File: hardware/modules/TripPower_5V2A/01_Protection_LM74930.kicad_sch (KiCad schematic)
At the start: 41 parts, among them J301 INPUT: VIN/RUN/GND, J302 OUT: PROT_UNFUSED/5V/GND, Q301 SQM10250E_GE3 250V CANDIDATE, Q302 BUK7Y4R8-60EX 60V CANDIDATE, U301 LM74930QRGERQ1

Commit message: feat(TripPower REV5): repurpose R317/R319 for RUN/AUTO sense; DNP legacy PNP EN path and BAS116
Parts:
- D305: value BAS116Q-7-F SERIES RUN SINK NO USB BACKFEED -> REV5 DNP LEGACY D305; now not fitted
- R316: value 22k EN PULLDOWN - VS ONLY PNP -> REV5 DNP LEGACY R316; now not fitted
- R317: value 4.7k RUN SERIES -> 1M 1% RUN_CMD TO SENSE2 - RUN ONLY; MPN (none) -> RC1206FR-071ML
- R318: value 68k PNP OUTPUT CURRENT LIMIT 202V -> REV5 DNP LEGACY R318; now not fitted
- R319: value 0R POPULATE FOR ALWAYS_ON -> 0R AUTO VS TO RUN_SENSE; DNP IN RUN; MPN (none) -> RC1206JR-070RL
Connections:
- net GND: no longer R319.2
- net RUN_BYPASS_NODE: no longer R319.1
- net VS_CLAMP: now also R319.1
- net RUN_BASE renamed RUN_SENSE
- net RUN_SENSE: now also R319.2
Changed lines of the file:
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@@
 (symbol (lib_id "Tripmaster_Sym:R") (at 149.86 275.59 0) (unit 1) (in_bom yes) (on_board yes) (dnp no) (property "Reference" "R314" (at 149.86 261.62 0) (effects (font (size 1 1)))) (property "Value" "3.3k 2512 PULSE CANDIDATE" (at 149.86 264.16 0) (effects (font (size 1 1)))) (property "Footprint" "Resistor_SMD:R_2512_6332Metric" (at 149.86 275.59 0) (effects (font (size 1.0 1.0)) (hide yes))) (property "MPN" "CRCW25123K30FKEGHP" (at 0 0 0) (effects (font (size 1 1)) (hide yes))) (pin "1") (pin "2") (instances (project "TripPower_5V2A" (path "/f1512578-cc72-4c26-bf70-dbbd00000001/f1512578-cc72-4c26-bf70-dbbd00000002" (reference "R314") (unit 1)))))
 (symbol (lib_id "Tripmaster_Sym:R") (at 234.95 275.59 0) (unit 1) (in_bom yes) (on_board yes) (dnp no) (property "Reference" "R315" (at 234.95 261.62 0) (effects (font (size 1 1)))) (property "Value" "3.3k 2512 PULSE CANDIDATE" (at 234.95 264.16 0) (effects (font (size 1 1)))) (property "Footprint" "Resistor_SMD:R_2512_6332Metric" (at 234.95 275.59 0) (effects (font (size 1.0 1.0)) (hide yes))) (property "MPN" "CRCW25123K30FKEGHP" (at 0 0 0) (effects (font (size 1 1)) (hide yes))) (pin "1") (pin "2") (instances (project "TripPower_5V2A" (path "/f1512578-cc72-4c26-bf70-dbbd00000001/f1512578-cc72-4c26-bf70-dbbd00000002" (reference "R315") (unit 1)))))
-(symbol (lib_id "Tripmaster_Sym:R") (at 320.04 275.59 0) (unit 1) (in_bom yes) (on_board yes) (dnp no) (property "Reference" "R316" (at 320.04 261.62 0) (effects (font (size 1 1)))) (property "Value" "22k EN PULLDOWN - VS ONLY PNP" (at 320.04 264.16 0) (effects (font (size 1 1)))) (property "Footprint" "Tripmaster:R_1206_3216" (at 320.04 275.59 0) (effects (font (size 1.0 1.0)) (hide yes))) (pin "1") (pin "2") (instances (project "TripPower_5V2A" (path "/f1512578-cc72-4c26-bf70-dbbd00000001/f1512578-cc72-4c26-bf70-dbbd00000002" (reference "R316") (unit 1)))))
-(symbol (lib_id "Tripmaster_Sym:R") (at 405.13 275.59 0) (unit 1) (in_bom yes) (on_board yes) (dnp no) (property "Reference" "R317" (at 405.13 261.62 0) (effects (font (size 1 1)))) (property "Value" "4.7k RUN SERIES" (at 405.13 264.16 0) (effects (font (size 1 1)))) (property "Footprint" "Tripmaster:R_1206_3216" (at 405.13 275.59 0) (effects (font (size 1.0 1.0)) (hide yes))) (pin "1") (pin "2") (instances (project "TripPower_5V2A" (path "/f1512578-cc72-4c26-bf70-dbbd00000001/f1512578-cc72-4c26-bf70-dbbd00000002" (reference "R317") (unit 1)))))
-(symbol (lib_id "Tripmaster_Sym:R") (at 490.22 275.59 0) (unit 1) (in_bom yes) (on_board yes) (dnp no) (property "Reference" "R318" (at 490.22 261.62 0) (effects (font (size 1 1)))) (property "Value" "68k PNP OUTPUT CURRENT LIMIT 202V" (at 490.22 264.16 0) (effects (font (size 1 1)))) (property "Footprint" "Tripmaster:R_1206_3216" (at 490.22 275.59 0) (effects (font (size 1.0 1.0)) (hide yes))) (pin "1") (pin "2") (instances (project "TripPower_5V2A" (path "/f1512578-cc72-4c26-bf70-dbbd00000001/f1512578-cc72-4c26-bf70-dbbd00000002" (reference "R318") (unit 1)))))
-(symbol (lib_id "Tripmaster_Sym:R") (at 64.77 299.72 0) (unit 1) (in_bom yes) (on_board yes) (dnp no) (property "Reference" "R319" (at 64.77 285.75 0) (effects (font (size 1 1)))) (property "Value" "0R POPULATE FOR ALWAYS_ON" (at 64.77 288.29 0) (effects (font (size 1 1)))) (property "Footprint" "Tripmaster:R_1206_3216" (at 64.77 299.72 0) (effects (font (size 1.0 1.0)) (hide yes))) (pin "1") (pin "2") (instances (project "TripPower_5V2A" (path "/f1512578-cc72-4c26-bf70-dbbd00000001/f1512578-cc72-4c26-bf70-dbbd00000002" (reference "R319") (unit 1)))))
+(symbol (lib_id "Tripmaster_Sym:R") (at 320.04 275.59 0) (unit 1) (in_bom yes) (on_board yes) (dnp yes) (property "Reference" "R316" (at 320.04 261.62 0) (effects (font (size 1 1)))) (property "Value" "REV5 DNP LEGACY R316" (at 320.04 264.16 0) (effects (font (size 1 1)))) (property "Footprint" "Tripmaster:R_1206_3216" (at 320.04 275.59 0) (effects (font (size 1.0 1.0)) (hide yes))) (pin "1") (pin "2") (instances (project "TripPower_5V2A" (path "/f1512578-cc72-4c26-bf70-dbbd00000001/f1512578-cc72-4c26-bf70-dbbd00000002" (reference "R316") (unit 1)))))
+(symbol (lib_id "Tripmaster_Sym:R") (at 405.13 275.59 0) (unit 1) (in_bom yes) (on_board yes) (dnp no) (property "Reference" "R317" (at 405.13 261.62 0) (effects (font (size 1 1)))) (property "Value" "1M 1% RUN_CMD TO SENSE2 - RUN ONLY" (at 405.13 264.16 0) (effects (font (size 1 1)))) (property "Footprint" "Tripmaster:R_1206_3216" (at 405.13 275.59 0) (effects (font (size 1.0 1.0)) (hide yes))) (property "MPN" "RC1206FR-071ML" (at 0 0 0) (effects (font (size 1 1)) (hide yes))) (pin "1") (pin "2") (instances (project "TripPower_5V2A" (path "/f1512578-cc72-4c26-bf70-dbbd00000001/f1512578-cc72-4c26-bf70-dbbd00000002" (reference "R317") (unit 1)))))
+(symbol (lib_id "Tripmaster_Sym:R") (at 490.22 275.59 0) (unit 1) (in_bom yes) (on_board yes) (dnp yes) (property "Reference" "R318" (at 490.22 261.62 0) (effects (font (size 1 1)))) (property "Value" "REV5 DNP LEGACY R318" (at 490.22 264.16 0) (effects (font (size 1 1)))) (property "Footprint" "Tripmaster:R_1206_3216" (at 490.22 275.59 0) (effects (font (size 1.0 1.0)) (hide yes))) (pin "1") (pin "2") (instances (project "TripPower_5V2A" (path "/f1512578-cc72-4c26-bf70-dbbd00000001/f1512578-cc72-4c26-bf70-dbbd00000002" (reference "R318") (unit 1)))))
+(symbol (lib_id "Tripmaster_Sym:R") (at 64.77 299.72 0) (unit 1) (in_bom yes) (on_board yes) (dnp no) (property "Reference" "R319" (at 64.77 285.75 0) (effects (font (size 1 1)))) (property "Value" "0R AUTO VS TO RUN_SENSE; DNP IN RUN" (at 64.77 288.29 0) (effects (font (size 1 1)))) (property "Footprint" "Tripmaster:R_1206_3216" (at 64.77 299.72 0) (effects (font (size 1.0 1.0)) (hide yes))) (property "MPN" "RC1206JR-070RL" (at 0 0 0) (effects (font (size 1 1)) (hide yes))) (pin "1") (pin "2") (instances (project "TripPower_5V2A" (path "/f1512578-cc72-4c26-bf70-dbbd00000001/f1512578-cc72-4c26-bf70-dbbd00000002" (reference "R319") (unit 1)))))
 (symbol (lib_id "Tripmaster_Sym:R") (at 149.86 299.72 0) (unit 1) (in_bom yes) (on_board yes) (dnp no) (property "Reference" "R320" (at 149.86 285.75 0) (effects (font (size 1 1)))) (property "Value" "100R dVdt-C SERIES (TI)" (at 149.86 288.29 0) (effects (font (size 1 1)))) (property "Footprint" "Tripmaster:R_1206_3216" (at 149.86 299.72 0) (effects (font (size 1.0 1.0)) (hide yes))) (pin "1") (pin "2") (instances (project "TripPower_5V2A" (path "/f1512578-cc72-4c26-bf70-dbbd00000001/f1512578-cc72-4c26-bf70-dbbd00000002" (reference "R320") (unit 1)))))
 (symbol (lib_id "Tripmaster_Sym:C") (at 234.95 299.72 0) (unit 1) (in_bom yes) (on_board yes) (dnp no) (property "Reference" "C301" (at 234.95 285.75 0) (effects (font (size 1 1)))) (property "Value" "47nF 50V TMR" (at 234.95 288.29 0) (effects (font (size 1 1)))) (property "Footprint" "Tripmaster:C_1206_3216" (at 234.95 299.72 0) (effects (font (size 1.0 1.0)) (hide yes))) (pin "1") (pin "2") (instances (project "TripPower_5V2A" (path "/f1512578-cc72-4c26-bf70-dbbd00000001/f1512578-cc72-4c26-bf70-dbbd00000002" (reference "C301") (unit 1)))))
@@
 (global_label "RUN_CMD" (shape bidirectional) (at 388.62 275.59 0) (effects (font (size 0.9 0.9)) (justify left)))
 (wire (pts (xy 416.56 275.59) (xy 421.64 275.59)) (stroke (width 0) (type default)))
-(global_label "RUN_BASE" (shape bidirectional) (at 421.64 275.59 0) (effects (font (size 0.9 0.9)) (justify left)))
+(global_label "RUN_SENSE" (shape bidirectional) (at 421.64 275.59 0) (effects (font (size 0.9 0.9)) (justify left)))
 (wire (pts (xy 478.79 275.59) (xy 473.71 275.59)) (stroke (width 0) (type default)))
 (global_label "PNP_OUT" (shape bidirectional) (at 473.71 275.59 0) (effects (font (size 0.9 0.9)) (justify left)))
@@
 (global_label "CTRL_EN" (shape bidirectional) (at 506.73 275.59 0) (effects (font (size 0.9 0.9)) (justify left)))
 (wire (pts (xy 53.34 299.72) (xy 48.26 299.72)) (stroke (width 0) (type default)))
-(global_label "RUN_BYPASS_NODE" (shape bidirectional) (at 48.26 299.72 0) (effects (font (size 0.9 0.9)) (justify left)))
+(global_label "VS_CLAMP" (shape bidirectional) (at 48.26 299.72 0) (effects (font (size 0.9 0.9)) (justify left)))
 (wire (pts (xy 76.2 299.72) (xy 81.28 299.72)) (stroke (width 0) (type default)))
-(global_label "GND" (shape bidirectional) (at 81.28 299.72 0) (effects (font (size 0.9 0.9)) (justify left)))
+(global_label "RUN_SENSE" (shape bidirectional) (at 81.28 299.72 0) (effects (font (size 0.9 0.9)) (justify left)))
 (wire (pts (xy 138.43 299.72) (xy 133.35 299.72)) (stroke (width 0) (type default)))
 (global_label "HGATE" (shape bidirectional) (at 133.35 299.72 0) (effects (font (size 0.9 0.9)) (justify left)))
@@
 (global_label "FAULT_OC_N" (shape bidirectional) (at 48.26 400.05 0) (effects (font (size 0.9 0.9)) (justify left)))
 (global_label "5V_OUT" (shape bidirectional) (at 81.28 400.05 0) (effects (font (size 0.9 0.9)) (justify left)))
-(symbol (lib_id "TripPower_Sym:BAS116Q_A1_K3_NC2") (at 151.13 400.05 0) (unit 1) (in_bom yes) (on_board yes) (dnp no)
+(symbol (lib_id "TripPower_Sym:BAS116Q_A1_K3_NC2") (at 151.13 400.05 0) (unit 1) (in_bom yes) (on_board yes) (dnp yes)
 (property "Reference" "D305" (at 151.13 384.81 0) (effects (font (size 1 1))))
-(property "Value" "BAS116Q-7-F SERIES RUN SINK NO USB BACKFEED" (at 151.13 388.62 0) (effects (font (size 1 1))))
+(property "Value" "REV5 DNP LEGACY D305" (at 151.13 388.62 0) (effects (font (size 1 1))))
 (property "Footprint" "Package_TO_SOT_SMD:SOT-23" (at 151.13 400.05 0) (effects (font (size 1 1)) (hide yes)))
 (pin "1") (pin "3") (pin "2")

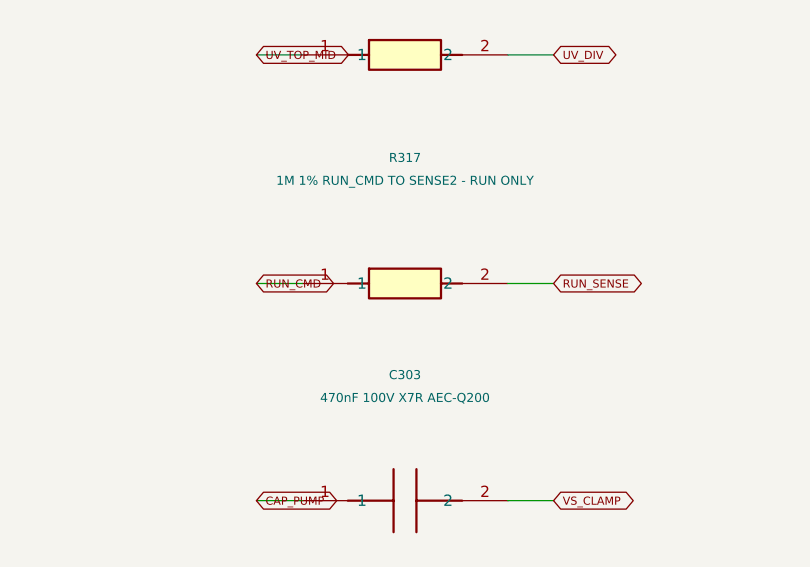
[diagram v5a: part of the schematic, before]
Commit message: feat(TripPower): DNP RUN-only R317 for AUTO standard assembly
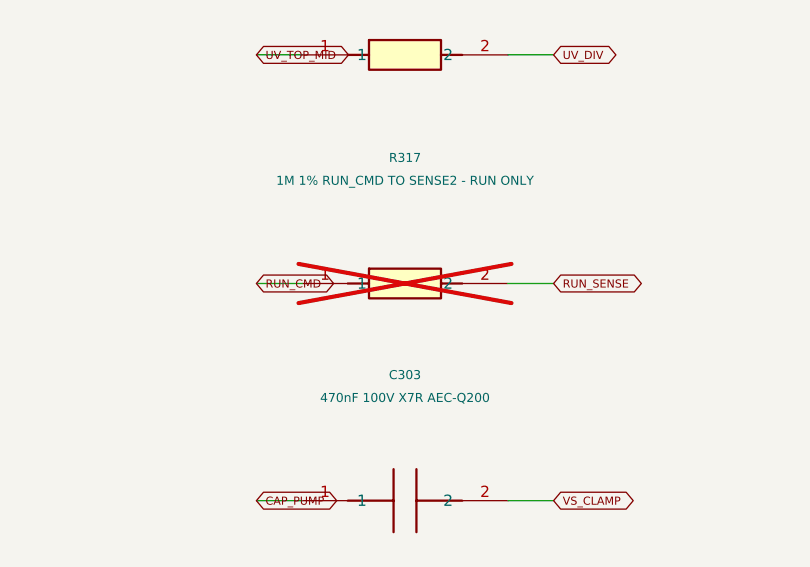
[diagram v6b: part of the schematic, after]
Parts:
- R317: now not fitted
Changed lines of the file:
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@@
 (symbol (lib_id "Tripmaster_Sym:R") (at 234.95 275.59 0) (unit 1) (in_bom yes) (on_board yes) (dnp no) (property "Reference" "R315" (at 234.95 261.62 0) (effects (font (size 1 1)))) (property "Value" "3.3k 2512 PULSE CANDIDATE" (at 234.95 264.16 0) (effects (font (size 1 1)))) (property "Footprint" "Resistor_SMD:R_2512_6332Metric" (at 234.95 275.59 0) (effects (font (size 1.0 1.0)) (hide yes))) (property "MPN" "CRCW25123K30FKEGHP" (at 0 0 0) (effects (font (size 1 1)) (hide yes))) (pin "1") (pin "2") (instances (project "TripPower_5V2A" (path "/f1512578-cc72-4c26-bf70-dbbd00000001/f1512578-cc72-4c26-bf70-dbbd00000002" (reference "R315") (unit 1)))))
 (symbol (lib_id "Tripmaster_Sym:R") (at 320.04 275.59 0) (unit 1) (in_bom yes) (on_board yes) (dnp yes) (property "Reference" "R316" (at 320.04 261.62 0) (effects (font (size 1 1)))) (property "Value" "REV5 DNP LEGACY R316" (at 320.04 264.16 0) (effects (font (size 1 1)))) (property "Footprint" "Tripmaster:R_1206_3216" (at 320.04 275.59 0) (effects (font (size 1.0 1.0)) (hide yes))) (pin "1") (pin "2") (instances (project "TripPower_5V2A" (path "/f1512578-cc72-4c26-bf70-dbbd00000001/f1512578-cc72-4c26-bf70-dbbd00000002" (reference "R316") (unit 1)))))
-(symbol (lib_id "Tripmaster_Sym:R") (at 405.13 275.59 0) (unit 1) (in_bom yes) (on_board yes) (dnp no) (property "Reference" "R317" (at 405.13 261.62 0) (effects (font (size 1 1)))) (property "Value" "1M 1% RUN_CMD TO SENSE2 - RUN ONLY" (at 405.13 264.16 0) (effects (font (size 1 1)))) (property "Footprint" "Tripmaster:R_1206_3216" (at 405.13 275.59 0) (effects (font (size 1.0 1.0)) (hide yes))) (property "MPN" "RC1206FR-071ML" (at 0 0 0) (effects (font (size 1 1)) (hide yes))) (pin "1") (pin "2") (instances (project "TripPower_5V2A" (path "/f1512578-cc72-4c26-bf70-dbbd00000001/f1512578-cc72-4c26-bf70-dbbd00000002" (reference "R317") (unit 1)))))
+(symbol (lib_id "Tripmaster_Sym:R") (at 405.13 275.59 0) (unit 1) (in_bom yes) (on_board yes) (dnp yes) (property "Reference" "R317" (at 405.13 261.62 0) (effects (font (size 1 1)))) (property "Value" "1M 1% RUN_CMD TO SENSE2 - RUN ONLY" (at 405.13 264.16 0) (effects (font (size 1 1)))) (property "Footprint" "Tripmaster:R_1206_3216" (at 405.13 275.59 0) (effects (font (size 1.0 1.0)) (hide yes))) (property "MPN" "RC1206FR-071ML" (at 0 0 0) (effects (font (size 1 1)) (hide yes))) (pin "1") (pin "2") (instances (project "TripPower_5V2A" (path "/f1512578-cc72-4c26-bf70-dbbd00000001/f1512578-cc72-4c26-bf70-dbbd00000002" (reference "R317") (unit 1)))))
 (symbol (lib_id "Tripmaster_Sym:R") (at 490.22 275.59 0) (unit 1) (in_bom yes) (on_board yes) (dnp yes) (property "Reference" "R318" (at 490.22 261.62 0) (effects (font (size 1 1)))) (property "Value" "REV5 DNP LEGACY R318" (at 490.22 264.16 0) (effects (font (size 1 1)))) (property "Footprint" "Tripmaster:R_1206_3216" (at 490.22 275.59 0) (effects (font (size 1.0 1.0)) (hide yes))) (pin "1") (pin "2") (instances (project "TripPower_5V2A" (path "/f1512578-cc72-4c26-bf70-dbbd00000001/f1512578-cc72-4c26-bf70-dbbd00000002" (reference "R318") (unit 1)))))
 (symbol (lib_id "Tripmaster_Sym:R") (at 64.77 299.72 0) (unit 1) (in_bom yes) (on_board yes) (dnp no) (property "Reference" "R319" (at 64.77 285.75 0) (effects (font (size 1 1)))) (property "Value" "0R AUTO VS TO RUN_SENSE; DNP IN RUN" (at 64.77 288.29 0) (effects (font (size 1 1)))) (property "Footprint" "Tripmaster:R_1206_3216" (at 64.77 299.72 0) (effects (font (size 1.0 1.0)) (hide yes))) (property "MPN" "RC1206JR-070RL" (at 0 0 0) (effects (font (size 1 1)) (hide yes))) (pin "1") (pin "2") (instances (project "TripPower_5V2A" (path "/f1512578-cc72-4c26-bf70-dbbd00000001/f1512578-cc72-4c26-bf70-dbbd00000002" (reference "R319") (unit 1)))))
